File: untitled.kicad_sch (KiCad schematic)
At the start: 14 parts, among them IC1 IP2326, J2 USB4105-GF-A

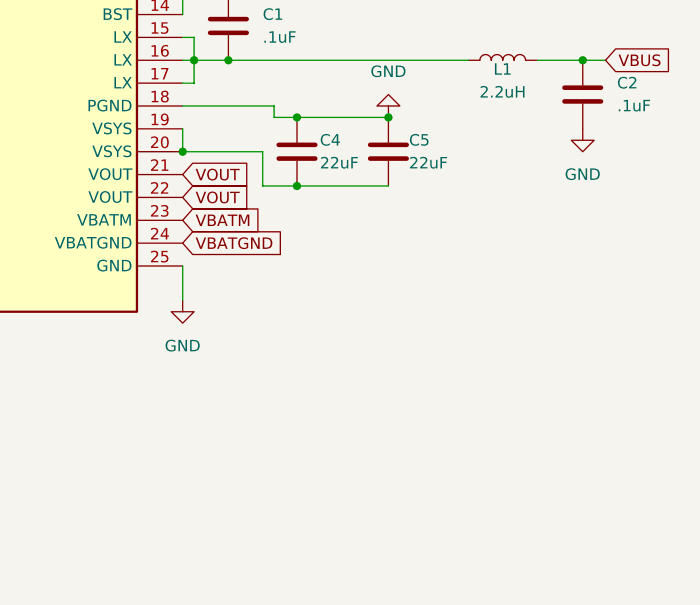
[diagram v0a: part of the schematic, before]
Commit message: Rev1 Update
Layout and traces done. 3d model done. Need to review layout placement and schematic. Change amp and dsp for lower cost??
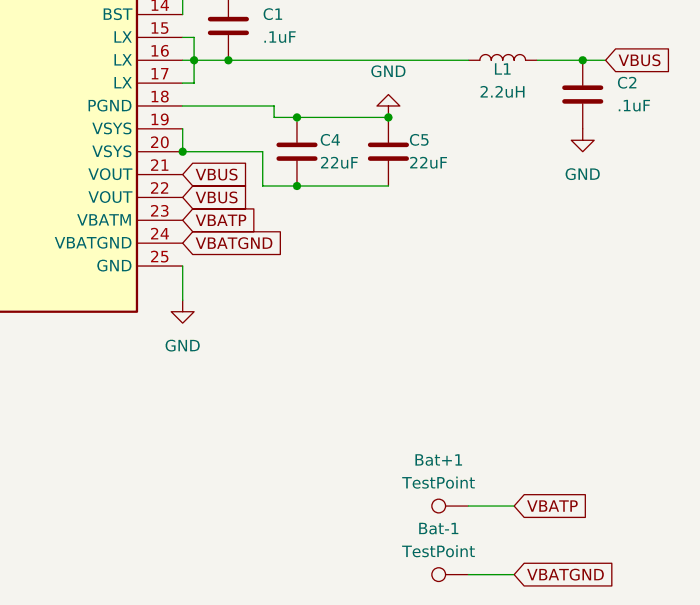
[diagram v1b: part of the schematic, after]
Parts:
- added Bat+1, Bat-1: TestPoint, TestPoint:TestPoint_Loop_D1.80mm_Drill1.0mm_Beaded, symbol Connector:TestPoint
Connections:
- net VOUT is gone; now on net VBUS: IC1.21 (VOUT), IC1.22 (VOUT)
- net VBATGND: now also Bat-1.1
- net VBATM renamed VBATP
- net VBATP: now also Bat+1.1
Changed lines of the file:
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@@
+	(wire
+		(pts
+			(xy 195.58 147.32) (xy 190.5 147.32)
+		)
+		(stroke
+			(width 0)
+			(type default)
+		)
+	)
 	(wire
 		(pts
@@
 		(pts
 			(xy 198.12 90.17) (xy 203.2 90.17)
+		)
+		(stroke
+			(width 0)
+			(type default)
+		)
+	)
+	(wire
+		(pts
+			(xy 195.58 139.7) (xy 190.5 139.7)
 		)
 		(stroke
@@
 		)
 	)
-	(global_label "VOUT"
+	(global_label "VBUS"
 		(shape input)
 		(at 158.75 102.87 0)
@@
 		)
 	)
-	(global_label "VBATM"
+	(global_label "VBATP"
+		(shape input)
+		(at 195.58 139.7 0)
+		(effects
+			(font
+				(size 1.27 1.27)
+			)
+			(justify left)
+		)
+		(property "Intersheetrefs" "${INTERSHEET_REFS}"
+			(at 195.58 139.7 0)
+			(effects
+				(font
+					(size 1.27 1.27)
+				)
+				(hide yes)
+			)
+		)
+	)
+	(global_label "VBATP"
 		(shape input)
 		(at 158.75 107.95 0)
@@
 	(global_label "VBATGND"
 		(shape input)
+		(at 195.58 147.32 0)
+		(effects
+			(font
+				(size 1.27 1.27)
+			)
+			(justify left)
+		)
+		(property "Intersheetrefs" "${INTERSHEET_REFS}"
+			(at 195.58 147.32 0)
+			(effects
+				(font
+					(size 1.27 1.27)
+				)
+				(hide yes)
+			)
+		)
+	)
+	(global_label "VBATGND"
+		(shape input)
 		(at 158.75 110.49 0)
 		(effects
@@
 		)
 	)
-	(global_label "VOUT"
+	(global_label "VBUS"
 		(shape input)
 		(at 158.75 105.41 0)
@@
 	)
 	(symbol
+		(lib_id "Connector:TestPoint")
+		(at 190.5 147.32 90)
+		(unit 1)
+		(exclude_from_sim no)
+		(in_bom yes)
+		(on_board yes)
+		(dnp no)
+		(fields_autoplaced yes)
+		(property "Reference" "Bat-1"
+			(at 187.198 142.24 90)
+			(effects
+				(font
+					(size 1.27 1.27)
+				)
+			)
+		)
+		(property "Value" "TestPoint"
+			(at 187.198 144.78 90)
+			(effects
+				(font
+					(size 1.27 1.27)
+				)
+			)
+		)
+		(property "Footprint" "TestPoint:TestPoint_Loop_D1.80mm_Drill1.0mm_Beaded"
+			(at 190.5 142.24 0)
+			(effects
+				(font
+					(size 1.27 1.27)
+				)
+				(hide yes)
+			)
+		)
+		(property "Datasheet" "~"
+			(at 190.5 142.24 0)
+			(effects
+				(font
+					(size 1.27 1.27)
+				)
+				(hide yes)
+			)
+		)
+		(property "Description" "test point"
+			(at 190.5 147.32 0)
+			(effects
+				(font
+					(size 1.27 1.27)
+				)
+				(hide yes)
+			)
+		)
+		(pin "1"
+		)
+		(instances
+			(project "Headphones"
+				(path "/7b9c80d0-1bd4-42a6-b78c-a7308fa454e7/f498f388-7f6e-4d36-81ce-25caa49a52f0"
+					(reference "Bat-1")
+					(unit 1)
+				)
+			)
+		)
+	)
+	(symbol
 		(lib_id "SamacSys_Parts:IP2326")
 		(at 109.22 74.93 0)
@@
 					(unit 1)
 				)
+			)
+		)
+	)
+	(symbol
+		(lib_id "Connector:TestPoint")
+		(at 190.5 139.7 90)
+		(unit 1)
+		(exclude_from_sim no)
+		(in_bom yes)
+		(on_board yes)
+		(dnp no)
+		(fields_autoplaced yes)
+		(property "Reference" "Bat+1"
+			(at 187.198 134.62 90)
+			(effects
+				(font
+					(size 1.27 1.27)
+				)
+			)
+		)
+		(property "Value" "TestPoint"
+			(at 187.198 137.16 90)
+			(effects
+				(font
+					(size 1.27 1.27)
+				)
+			)
+		)
+		(property "Footprint" "TestPoint:TestPoint_Loop_D1.80mm_Drill1.0mm_Beaded"
+			(at 190.5 134.62 0)
+			(effects
+				(font
+					(size 1.27 1.27)
+				)
+				(hide yes)
+			)
+		)
+		(property "Datasheet" "~"
+			(at 190.5 134.62 0)
+			(effects
+				(font
+					(size 1.27 1.27)
+				)
+				(hide yes)
+			)
+		)
+		(property "Description" "test point"
+			(at 190.5 139.7 0)
+			(effects
+				(font
+					(size 1.27 1.27)
+				)
+				(hide yes)
+			)
+		)
+		(pin "1"
+		)
+		(instances
+			(project "Headphones"
+				(path "/7b9c80d0-1bd4-42a6-b78c-a7308fa454e7/f498f388-7f6e-4d36-81ce-25caa49a52f0"
+					(reference "Bat+1")
+					(unit 1)
+				)
